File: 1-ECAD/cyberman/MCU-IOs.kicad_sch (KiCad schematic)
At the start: 3 parts, among them U1 ESP32-S3R16V

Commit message: update power sche
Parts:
- added L2: 24 nH, symbol Device:L
- added X1: 40 MHz, symbol 0_crystal_smd:R940000171
- U1: Supplier 1 (none) -> Mouser; Supplier PN 1 (none) -> 356-ESP32-S3R16V
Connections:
- net GND: now also X1.2, X1.4
- net at U1.53 (XTAL_N): now also X1.3
- net at U1.54 (XTAL_P): now also L2.2
- new net: L2.1, X1.1
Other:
- moved on the sheet: C11, R1

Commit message: power
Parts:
- added C12, C13: C, symbol Device:C
- X1: Manufacturer (none) -> TROQ; Manufacturer PN (none) -> R940000171
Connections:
- net GND: now also C12.2, C13.2
- net at U1.53 (XTAL_N), X1.3: now also C13.1
- net at L2.1, X1.1: now also C12.1
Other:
- moved on the sheet: L2

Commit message: microSD and LCD connector
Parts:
- U1: Manufacturer (none) -> Espressif; Manufacturer PN (none) -> ESP32-S3R16V; kode PN (none) -> DOTU001
- X1: kode PN (none) -> DOTX001
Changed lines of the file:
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@@
+			)
+		)
+		(property "kode PN" "DOTU001"
+			(at 170.18 29.21 0)
+			(effects
+				(font
+					(size 1.27 1.27)
+				)
+				(hide yes)
+			)
+		)
+		(property "Manufacturer" "Espressif"
+			(at 170.18 29.21 0)
+			(effects
+				(font
+					(size 1.27 1.27)
+				)
+				(hide yes)
+			)
+		)
+		(property "Manufacturer PN" "ESP32-S3R16V"
+			(at 170.18 29.21 0)
+			(effects
+				(font
+					(size 1.27 1.27)
+				)
+				(hide yes)
 			)
 		)
@@
 			(at 135.89 58.42 0)
 			(effects
+				(font
+					(size 1.27 1.27)
+				)
+				(hide yes)
+			)
+		)
+		(property "kode PN" "DOTX001"
+			(at 135.89 58.42 0)
+			(effects

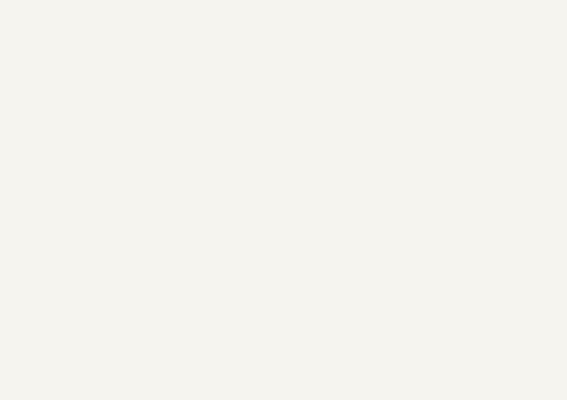
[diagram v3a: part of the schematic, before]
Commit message: add mic and speaker
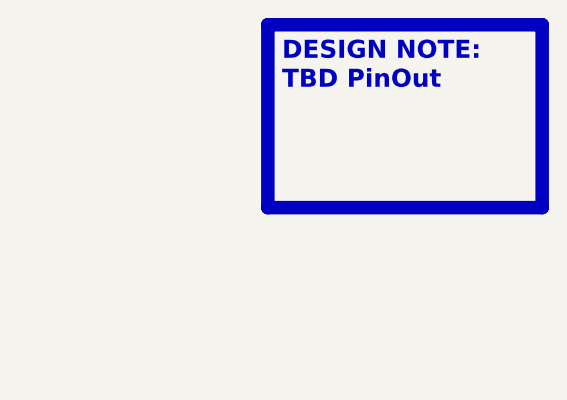
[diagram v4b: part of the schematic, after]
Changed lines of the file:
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@@
+		)
+	)
+	(text_box "DESIGN NOTE:\nTBD PinOut"
+		(exclude_from_sim no)
+		(at 241.3 26.67 0)
+		(size 30.48 20.32)
+		(stroke
+			(width 1.5)
+			(type solid)
+			(color 255 0 0 1)
+		)
+		(fill
+			(type none)
+		)
+		(effects
+			(font
+				(face "Times New Roman")
+				(size 2 2)
+				(thickness 0.4)
+				(bold yes)
+				(color 255 0 0 1)
+			)
+			(justify left top)
 		)
 	)

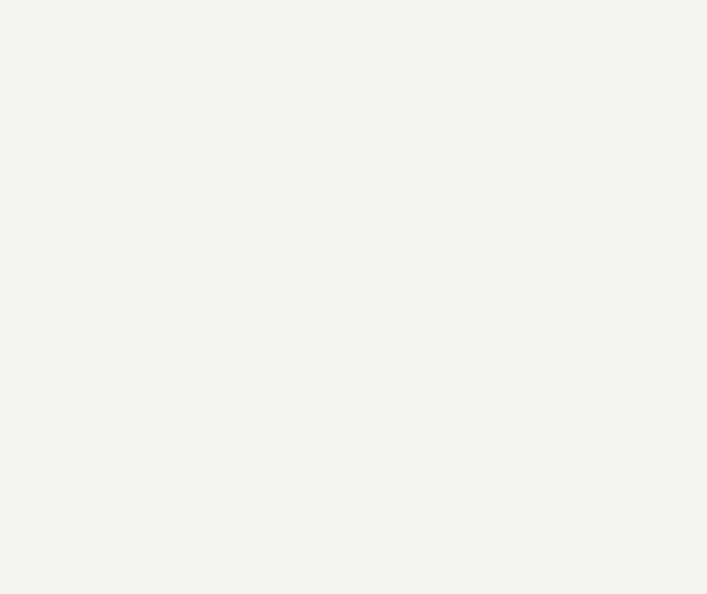
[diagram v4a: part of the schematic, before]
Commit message: add bus and display connection
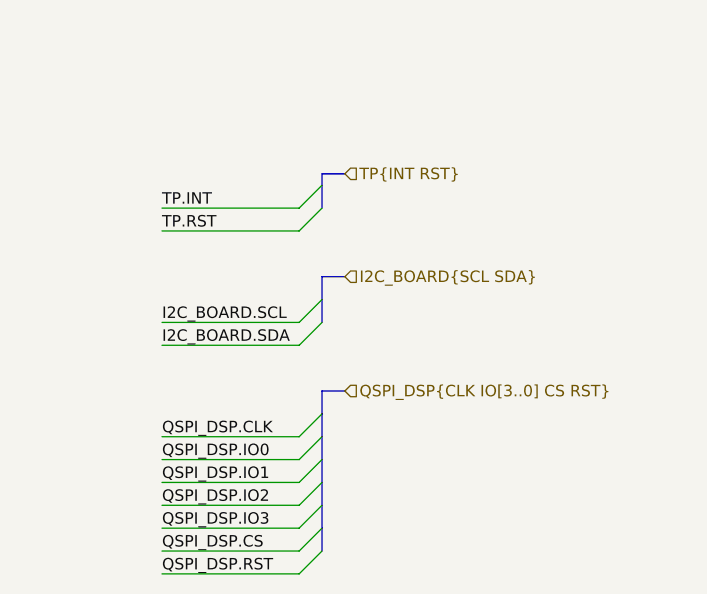
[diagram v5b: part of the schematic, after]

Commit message: hey
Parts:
- added C46, C47: 18pF, symbol Device:C
- added C48: 10uF, symbol Device:C
- added R28: 499R, symbol Device:R
- added R29, R30: 22R, symbol Device:R
- added R31, R32: 5.1k, symbol Device:R
- added U15: W25Q128JWPIQ, symbol 0_CI_smd:W25Q128JWPIQ
- added U16: 1054500101, symbol 0_connector_smd:1054500101
- U1: kode_PN DOTU001 -> (none)
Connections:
- net GND: now also C46.2, C47.2, C48.2, R31.2, R32.2, U15.4 (GND), U16.A1 (GND), U16.A12 (GND), U16.B1 (GND), U16.B12 (GND), U16.S1 (SHIELD), U16.S2 (SHIELD), U16.S3 (SHIELD), U16.S4 (SHIELD)
- net USB_D-: now reaches U1.25 (GPIO19)
- net USB_D-: now also R30.2
- net USB_D+: now reaches U1.26 (GPIO20)
- net USB_D+: now also R29.2
- net SPIHD: now reaches U1.30 (SPIHD)
- net SPIHD: now also U15.7 (IO3)
- net SPIWP: now reaches U1.31 (SPIWP)
- net SPIWP: now also U15.3 (IO2)
- net SPICS0: now reaches U1.32 (SPICS0)
- net SPICS0: now also U15.1 (~{CS})
- net SPICLK: now reaches U1.33 (SPICLK)
- net SPICLK: now also U15.6 (CLK)
- net SPIQ: now reaches U1.34 (SPIQ)
- net SPIQ: now also U15.2 (DO(IO1))
- net SPID: now reaches U1.35 (SPID)
- net SPID: now also U15.5 (DI(IO0))
- net GPIO39: now reaches U1.44 (MTCK)
- net GPIO40: now reaches U1.45 (MTDO)
- net GPIO41: now reaches U1.47 (MTDI)
- net GPIO42: now reaches U1.48 (MTMS)
- net at U1.49 (U0TXD): now also R28.2
- net U0RXD: now reaches U1.50 (U0RXD)
- new net: C47.1, R30.1, U16.A7 (D-), U16.B7 (D-)
- new net: R32.1, U16.A5 (CC1)
- new net: C46.1, R29.1, U16.A6 (D+), U16.B6 (D+)
- new net: R31.1, U16.B5 (CC2)
- new net U0TXD: R28.1
- new net VDD_SPI: U15.8 (VCC)
- new net VUSB_5V: C48.1, U16.A4 (VBUS), U16.A9 (VBUS), U16.B4 (VBUS), U16.B9 (VBUS)
- no-connect marks 0 -> 17
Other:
- note added: "OUT"
- moved on the sheet: C11, C12, C13, L2, R1, X1

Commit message: connections
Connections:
- net BOARD_I2C.SCL: now also U1.19 (GPIO14)
- net BOARD_I2C.SDA: now also U1.21 (XTAL_32K_P)
- net DSP.CS: now also U1.12 (GPIO7)
- net DSP.RST: now also U1.13 (GPIO8)
- net I2S.SCK: now also U1.43 (GPIO38)
- net I2S.SD: now also U1.51 (GPIO45)
- net I2S.WS: now also U1.52 (GPIO46)
- net QSPI.CLK: now also U1.14 (GPIO9)
- net QSPI.IO0: now also U1.15 (GPIO10)
- net QSPI.IO1: now also U1.16 (GPIO11)
- net QSPI.IO2: now also U1.17 (GPIO12)
- net QSPI.IO3: now also U1.18 (GPIO13)
- net SD.CD: now also U1.42 (GPIO37)
- net SD.CS: now also U1.22 (XTAL_32K_N)
- net SD.CLK: now reaches U1.23 (GPIO17)
- net SD.MOSI: now reaches U1.24 (GPIO18)
- net SD.MISO: now reaches U1.27 (GPIO21)
- net BUTTON.SELECT: now reaches U1.36 (SPICLK_N)
- net BUTTON.BACK: now reaches U1.37 (SPICLK_P)
- net BUTTON.LEFT: now reaches U1.38 (GPIO33)
- net BUTTON.TOP: now reaches U1.39 (GPIO34)
- net BUTTON.RIGHT: now reaches U1.40 (GPIO35)
- net BUTTON.BOTTOM: now reaches U1.41 (GPIO36)
- no-connect marks 17 -> 10
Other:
- note added: "1.8V"

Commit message: esp and usbc footprints
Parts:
- U1: footprint (none) -> 0_mcu_espressif:ESP32-S3R16V; kode_PN (none) -> DOTU001
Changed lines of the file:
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@@
 			)
 		)
-		(property "Footprint" ""
+		(property "Footprint" "0_mcu_espressif:ESP32-S3R16V"
 			(at 171.45 12.7 0)
 			(effects
@@
 			(at 165.1 25.4 0)
 			(effects
+				(font
+					(size 1.27 1.27)
+				)
+				(hide yes)
+			)
+		)
+		(property "kode_PN" "DOTU001"
+			(at 165.1 25.4 0)
+			(effects
